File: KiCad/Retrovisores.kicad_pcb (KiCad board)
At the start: 2 copper layers, 68 parts, among them J1 Conn_01x02_Pin, J10 Conn_01x07_Pin, J11 Conn_01x02_Pin, J2 DE9_Pins, J3 Conn_01x04_Pin, J4 DE9_Pins, J5 Conn_01x02_Pin, J6 Conn_01x02_Pin, J7 Conn_01x02_Pin, J8 Conn_PIC_ICSP_ICD, J9 Conn_01x04_Pin, K2 Relay_SPDT, Q14 AO3400A, Q15 AO3401A, Q16 AO3400A, Q17 AO3401A, Q18 AO3400A, Q19 AO3401A, Q20 AO3400A, Q21 AO3401A, Q22 AO3400A, Q23 AO3401A, Q24 AO3400A, Q25 AO3401A, Q27 AO3400A, SW1 SW_Push, SW2 SW_Push, SW3 SW_Push, SW4 SW_Push, SW6 SW_Nidec_CAS-120A1, U2 SN65HVD232, U4 LT1117-3.3, U5 TSR3-2450N, U7 PIC32MX250F128D-IPT, Y1 Crystal

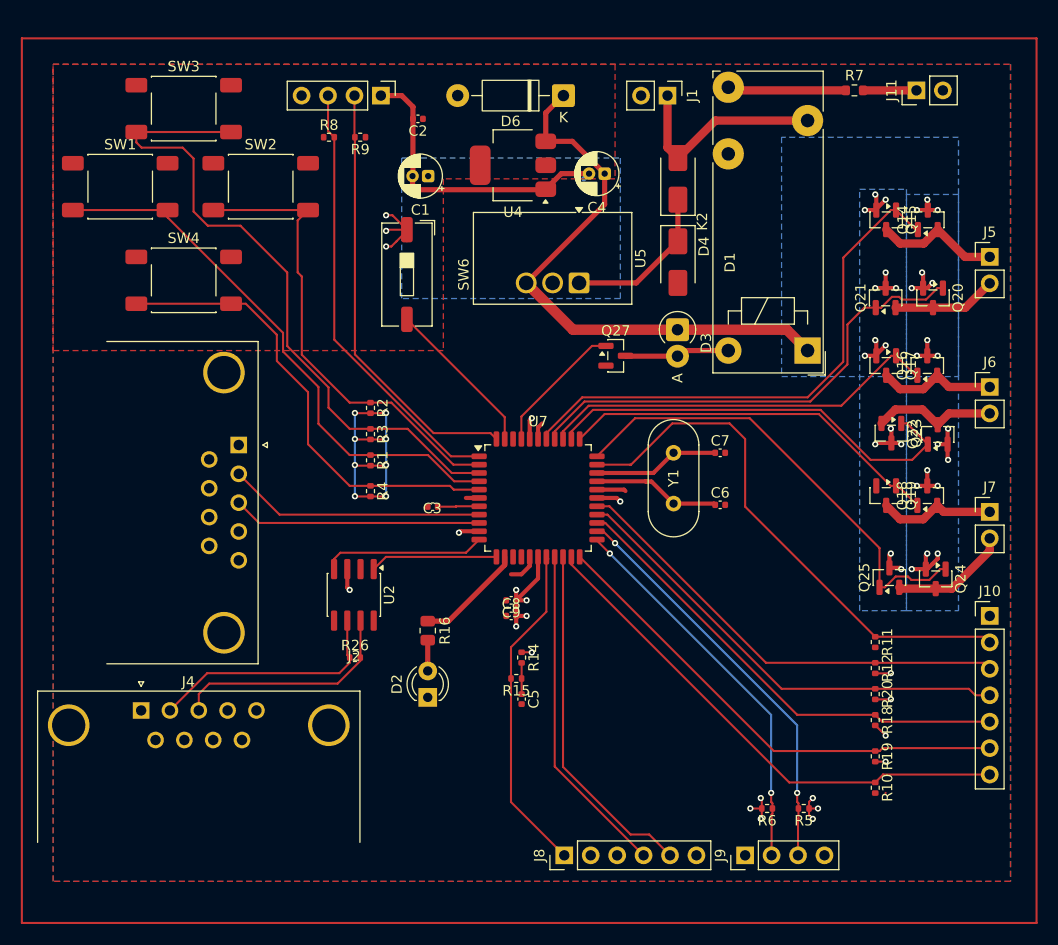
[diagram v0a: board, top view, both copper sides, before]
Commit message: habia un par de cosas mal en las reglas de diseño
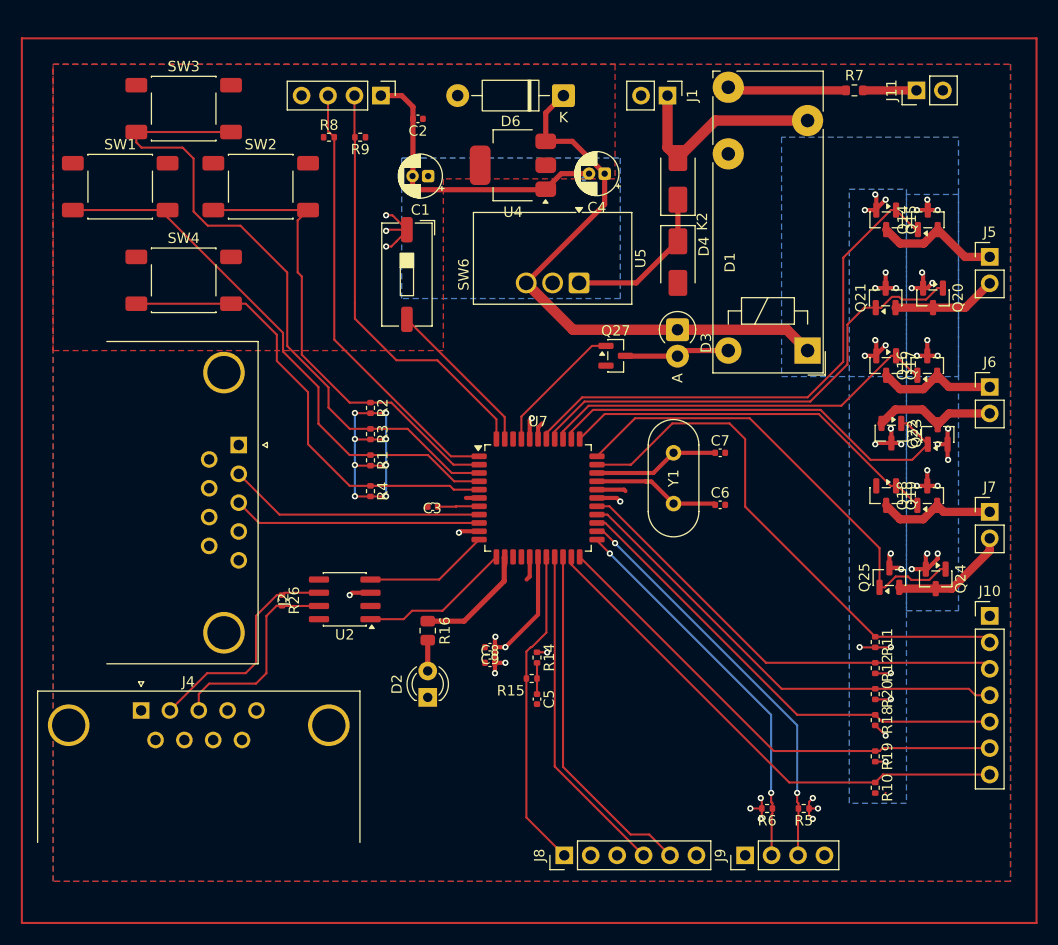
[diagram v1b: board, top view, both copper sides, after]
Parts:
- moved R26 8.90 mm to (110.0, 79.0), turned to -90 degrees
- moved C8 4.94 mm to (130.0, 85.0)
- moved C9 4.94 mm to (130.0, 83.5)
- moved R15 1.48 mm to (134.0, 86.5)
- moved C5 1.48 mm to (134.5, 88.5)
- moved R14 1.48 mm to (134.5, 84.5)
- moved U2 0.98 mm to (116.0, 78.9), turned to 180 degrees
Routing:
- net VCC: track 35.0 -> 39.9 mm
- net U: track 68.5 -> 64.5 mm
- net DCAN: track 15.7 -> 12.0 mm
- net Net-(U2-CANH): track 22.3 -> 19.9 mm
- net GND: track 90.0 -> 92.3 mm, vias 26 -> 28
- net RCAN: track 12.3 -> 14.6 mm
- net Net-(U2-CANL): track 23.3 -> 21.6 mm
- net Net-(U7-RA7): track 10.4 -> 12.1 mm
- net MCLR: track 32.5 -> 31.3 mm
- net KLKI2C: track 41.9 -> 41.0 mm

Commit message: ajustado ancho de pista de Vbat y 5V
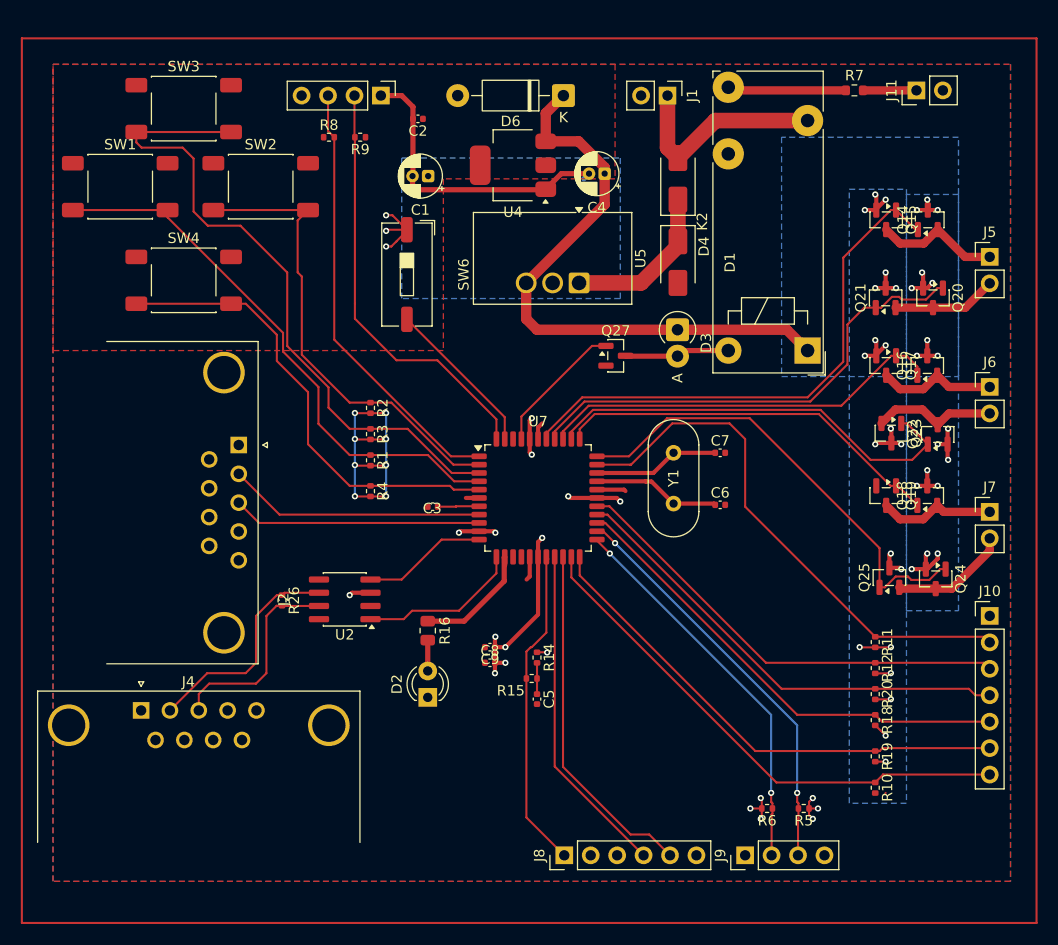
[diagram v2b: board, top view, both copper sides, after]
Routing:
- net VCC: track 39.9 -> 47.9 mm, vias 18 -> 22
- net 5V: track 78.2 -> 80.6 mm
- net FC5: track 47.2 -> 48.3 mm
- net RCAN: track 14.6 -> 15.5 mm
- net FC6: track 49.9 -> 50.7 mm
- net SDU1: track 38.6 -> 39.2 mm
- net OP: track 37.1 -> 37.6 mm

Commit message: versión casi final del enrutado
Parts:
- removed R7: 4.7k, Resistor_SMD:R_0603_1608Metric
- moved J8 12.9 mm to (125.5, 98.0)
- moved R5 12.4 mm to (149.0, 93.5)
- moved R6 12.4 mm to (145.5, 93.5)
- moved J9 11.4 mm to (144.5, 98.0)
- moved C2 7.76 mm to (123.5, 40.5), turned to -90 degrees
- moved J4 4.53 mm to (101.0, 89.1)
- moved SW1 4.12 mm to (98.5, 40.2)
- moved SW2 4.12 mm to (112.0, 40.2)
- moved SW3 4.12 mm to (104.5, 32.8)
- moved SW4 4.12 mm to (104.5, 49.2)
- moved J11 3.96 mm to (167.0, 30.0)
- moved C1 3.78 mm to (126.0, 35.0)
- moved J3 3.12 mm to (122.6, 30.5)
- moved R8 3.12 mm to (117.6, 34.5)
- moved R9 3.12 mm to (120.6, 34.5)
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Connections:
- net Net-(U2-CANH) renamed CAN_+
- net Net-(U2-CANL) renamed CAN_-
- K2 pad 14: Net-(K2-Pad14) -> Net-(J11-Pin_1)
- Q14 pad 3: 5V -> VBAT
- Q16 pad 3: 5V -> VBAT
- Q18 pad 3: 5V -> VBAT
- Q20 pad 2: 5V -> VBAT
- Q22 pad 2: 5V -> VBAT
- Q24 pad 2: 5V -> VBAT
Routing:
- net 5V: track 80.6 -> 55.5 mm, vias 18 -> 0
- net VBAT: track 20.4 -> 44.1 mm, vias 0 -> 18
- net GND: track 92.3 -> 71.4 mm, vias 28 -> 31
- net Net-(K2-Pad14): track 11.4 -> 0.00 mm
- net PGC: track 34.0 -> 23.7 mm
- net SCL: track 39.5 -> 29.8 mm
- net SDA: track 37.4 -> 28.1 mm
- net Net-(J11-Pin_1): track 5.14 -> 14.2 mm
- net PGD: track 32.2 -> 24.5 mm
- net CAN_-: track 21.6 -> 16.9 mm
- net L: track 45.0 -> 40.9 mm
- net MCLR: track 31.3 -> 27.6 mm
- net D: track 44.7 -> 41.3 mm
- net CAN_+: track 19.9 -> 16.7 mm
- net RX: track 24.7 -> 27.1 mm
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- added copper zone on B.Cu, net VBAT
- removed copper zone on B.Cu, net 5V
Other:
- board outline added: 92 x 77 mm

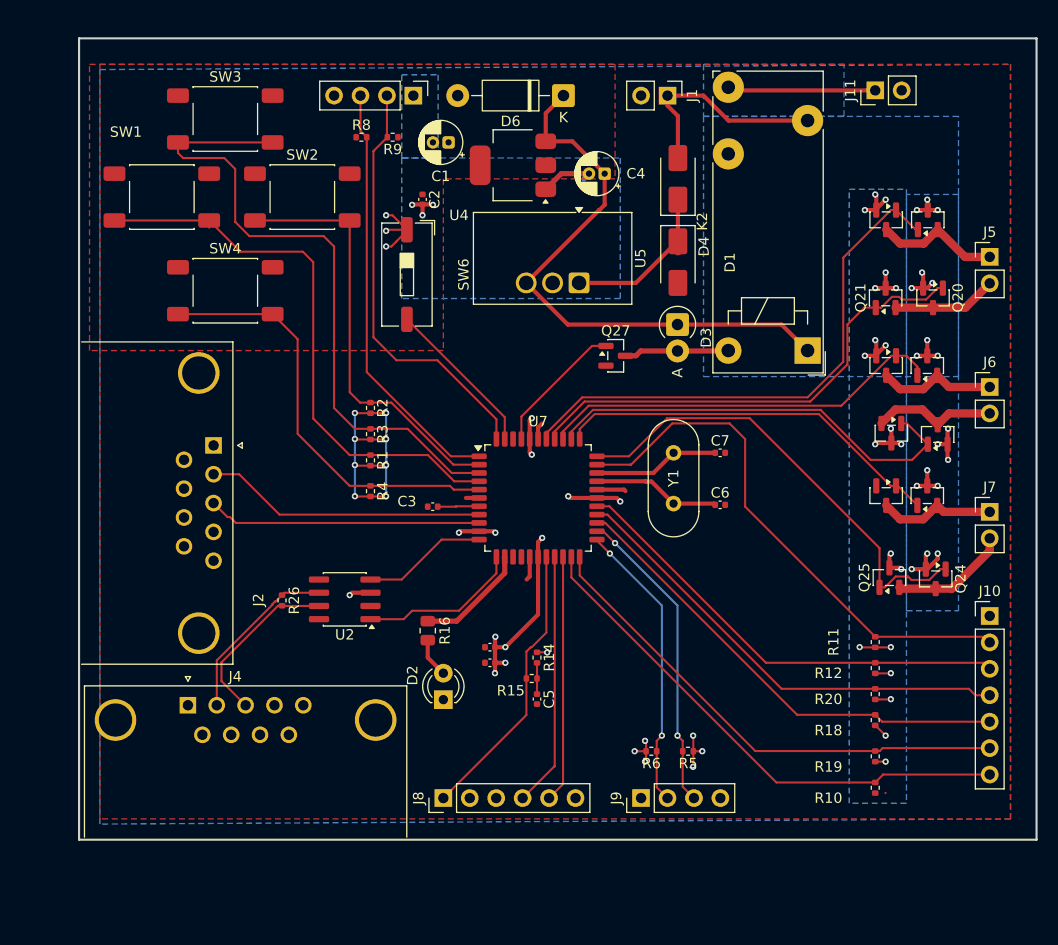
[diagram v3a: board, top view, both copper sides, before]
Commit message: añadido test points y solucionado un error con gnd en alimentación
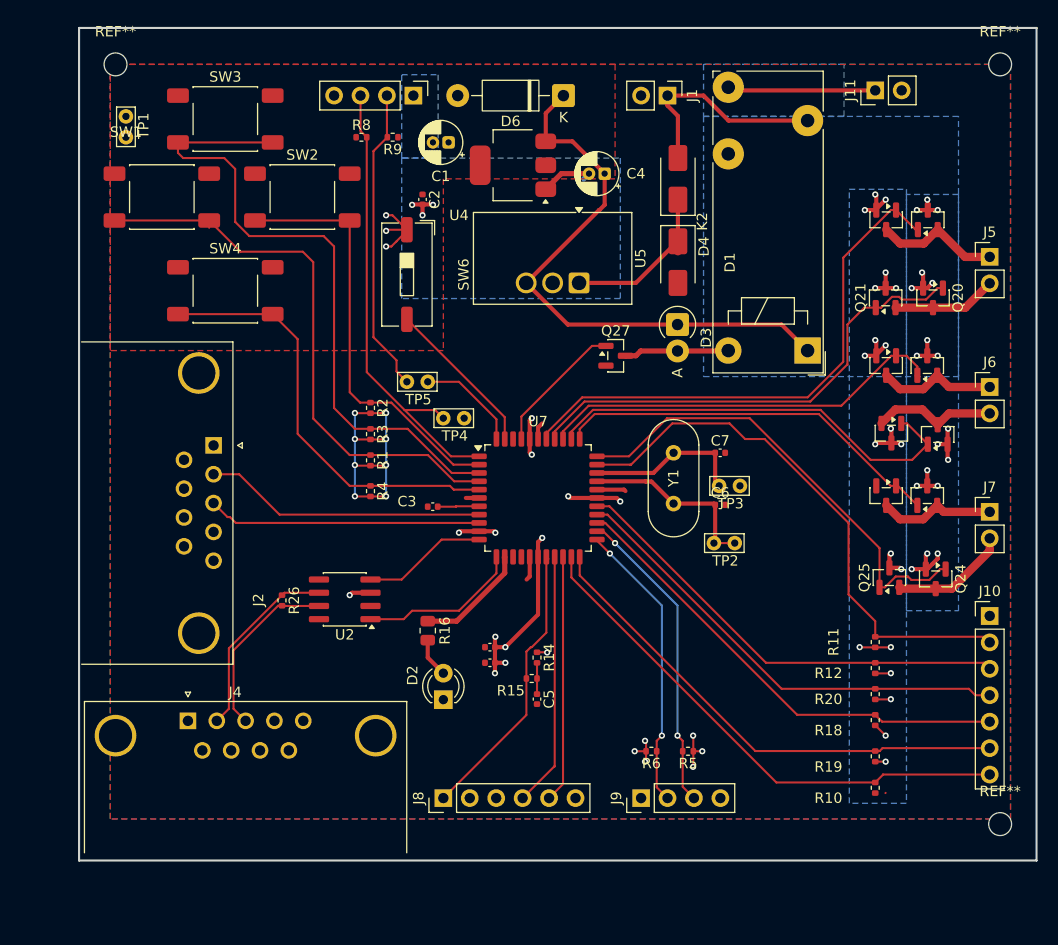
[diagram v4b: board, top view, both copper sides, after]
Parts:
- added REF**: MountingHole_2.2mm_M2, MountingHole:MountingHole_2.2mm_M2, F.Cu at (179.0, 100.5)
- added REF**: MountingHole_2.2mm_M2, MountingHole:MountingHole_2.2mm_M2, F.Cu at (94.0, 27.5)
- added REF**: MountingHole_2.2mm_M2, MountingHole:MountingHole_2.2mm_M2, F.Cu at (179.0, 27.5)
- added TP1: TestPoint, TestPoint:TestPoint_Bridge_Pitch2.0mm_Drill0.7mm, F.Cu at (95.0, 34.5)
- added TP2: TestPoint, TestPoint:TestPoint_Bridge_Pitch2.0mm_Drill0.7mm, F.Cu at (151.5, 73.5)
- added TP3: TestPoint, TestPoint:TestPoint_Bridge_Pitch2.0mm_Drill0.7mm, F.Cu at (152.0, 68.0)
- added TP4: TestPoint, TestPoint:TestPoint_Bridge_Pitch2.0mm_Drill0.7mm, F.Cu at (125.5, 61.5)
- added TP5: TestPoint, TestPoint:TestPoint_Bridge_Pitch2.0mm_Drill0.7mm, F.Cu at (122.0, 58.0)
- moved J4 1.50 mm to (101.0, 90.6)
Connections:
- J1 pad 2: GNDPWR -> GND
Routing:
- net OSC1: track 12.3 -> 18.7 mm
- net DI2C: track 41.0 -> 45.0 mm
- net OSC2: track 12.2 -> 15.5 mm
- net CAN_-: track 16.9 -> 18.3 mm
- net KLKI2C: track 40.8 -> 39.4 mm
- net FCR: track 51.9 -> 53.0 mm
- net CAN_+: track 16.7 -> 17.3 mm
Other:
- board size 92 x 77 mm -> 92 x 80 mm

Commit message: Eliminado los errores del DRC
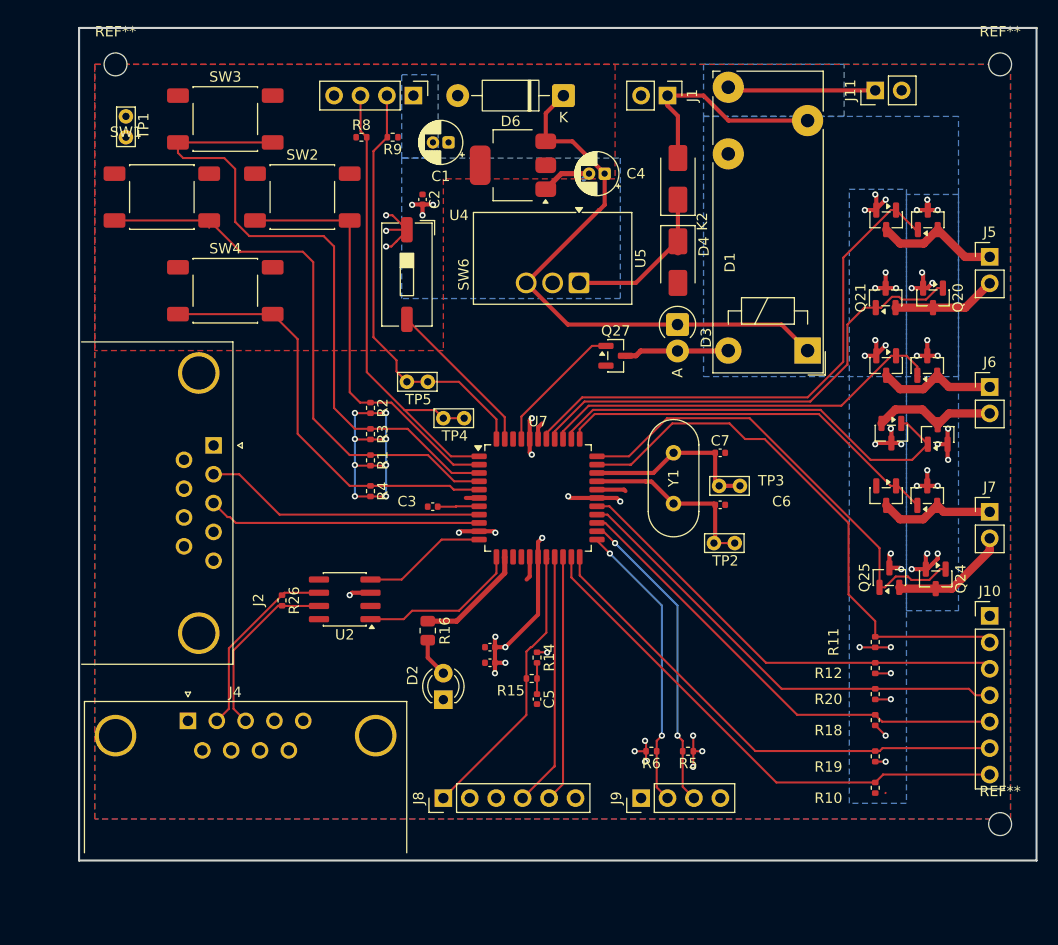
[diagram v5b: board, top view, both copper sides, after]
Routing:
- net OSC2: track 15.5 -> 17.5 mm
- net KLKI2C: track 39.4 -> 41.4 mm
- net DI2C: track 45.0 -> 47.0 mm
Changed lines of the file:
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@@
 		(tags "capacitor")
 		(property "Reference" "C6"
-			(at 0 -1.16 0)
+			(at 5.9 -0.325 0)
 			(layer "F.SilkS")
 			(effects
@@
 		(tags "test point wire loop")
 		(property "Reference" "TP3"
-			(at 1.1 1.7 0)
+			(at 5 -0.5 0)
 			(layer "F.SilkS")
 			(effects
@@
 	)
 	(segment
-		(start 151.62 67.62)
-		(end 152 68)
+		(start 152 68)
+		(end 154 68)
 		(width 0.4)
 		(layer "F.Cu")
@@
 	)
 	(segment
+		(start 151.62 67.62)
+		(end 152 68)
+		(width 0.4)
+		(layer "F.Cu")
+		(net 7)
+	)
+	(segment
 		(start 145.6825 66.7625)
 		(end 140.2625 66.7625)
@@
 	)
 	(segment
+		(start 125.5 61.5)
+		(end 127.5 61.5)
+		(width 0.2)
+		(layer "F.Cu")
+		(net 53)
+	)
+	(segment
 		(start 117.54 33.9)
 		(end 118.14 34.5)
@@
 	)
 	(segment
+		(start 122 58)
+		(end 124 58)
+		(width 0.2)
+		(layer "F.Cu")
+		(net 54)
+	)
+	(segment
 		(start 130.6 63.5)
 		(end 130.6 61.6)
@@
 		(polygon
 			(pts
-				(xy 93.5 27.5) (xy 180 27.5) (xy 180 100) (xy 93.5 100)
+				(xy 92 27.5) (xy 180 27.5) (xy 180 100) (xy 92 100)
 			)
 		)
@@
 		(polygon
 			(pts
-				(xy 93.5 27.5) (xy 142 27.5) (xy 142 38.5) (xy 125.5 38.5) (xy 125.5 55) (xy 93.5 55)
+				(xy 92 27.5) (xy 142 27.5) (xy 142 38.5) (xy 125.5 38.5) (xy 125.5 55) (xy 92 55)
 			)
 		)
@@
 		(polygon
 			(pts
-				(xy 93.5 27.5) (xy 180 27.5) (xy 180 100) (xy 93.5 100)
+				(xy 92 27.5) (xy 180 27.5) (xy 180 100) (xy 92 100)
 			)
 		)

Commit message: ultima versió PCB
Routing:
- net VBAT: track 44.1 -> 42.1 mm
- net Net-(D1-K): track 16.6 -> 15.2 mm
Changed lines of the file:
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@@
 	)
 	(segment
-		(start 148.04 44.5)
-		(end 148.04 44.96)
-		(width 1.5)
-		(layer "F.Cu")
-		(net 8)
-	)
-	(segment
-		(start 148 44.5)
-		(end 144 48.5)
-		(width 0.4)
-		(layer "F.Cu")
-		(net 8)
-	)
-	(segment
-		(start 144 48.5)
-		(end 138.54 48.5)
-		(width 0.4)
-		(layer "F.Cu")
-		(net 8)
-	)
-	(segment
-		(start 148.04 44.5)
-		(end 148.04 45.46)
-		(width 0.8)
+		(start 138.54 48.5)
+		(end 144.04 48.5)
+		(width 1)
 		(layer "F.Cu")
 		(net 8)
@@
 		(start 148.04 40.5)
 		(end 148.04 44.5)
-		(width 0.4)
+		(width 1)
 		(layer "F.Cu")
 		(net 8)
@@
 	)
 	(segment
+		(start 144.04 48.5)
+		(end 148.04 44.5)
+		(width 1)
+		(layer "F.Cu")
+		(net 8)
+	)
+	(segment
 		(start 171.6 47.6)
 		(end 171.5 47.5)
@@
 	)
 	(segment
-		(start 152.9 32.9)
-		(end 150.5 30.5)
-		(width 0.4)
-		(layer "F.Cu")
-		(net 9)
-	)
-	(segment
 		(start 171.6 49)
 		(end 171.6 47.6)
@@
 		(end 171 41.5)
 		(width 0.4)
+		(layer "F.Cu")
+		(net 9)
+	)
+	(segment
+		(start 147.04 32.04)
+		(end 148.04 33.04)
+		(width 1)
 		(layer "F.Cu")
 		(net 9)
@@
 	)
 	(segment
+		(start 151 32.9)
+		(end 160.5 32.9)
+		(width 1)
+		(layer "F.Cu")
+		(net 9)
+	)
+	(segment
 		(start 173.95 65.45)
 		(end 174 65.5)
@@
 	)
 	(segment
-		(start 148.04 32.46)
-		(end 148.04 36.5)
-		(width 0.4)
-		(layer "F.Cu")
-		(net 9)
-	)
-	(segment
 		(start 172.05 41.5)
 		(end 172.05 40.55)
@@
 	)
 	(segment
-		(start 160.5 32.9)
-		(end 152.9 32.9)
-		(width 0.4)
-		(layer "F.Cu")
-		(net 9)
-	)
-	(segment
 		(start 173.95 62.55)
 		(end 174 62.5)
@@
 	)
 	(segment
-		(start 147.04 31.46)
-		(end 148.04 32.46)
-		(width 0.4)
-		(layer "F.Cu")
-		(net 9)
-	)
-	(segment
 		(start 172.05 40.55)
 		(end 172 40.5)
@@
 	)
 	(segment
-		(start 150.5 30.5)
-		(end 147.04 30.5)
-		(width 0.4)
-		(layer "F.Cu")
-		(net 9)
-	)
-	(segment
 		(start 171.860266 76)
 		(end 171.860266 74.639734)
@@
 	)
 	(segment
+		(start 148.04 33.04)
+		(end 148.04 36.5)
+		(width 1)
+		(layer "F.Cu")
+		(net 9)
+	)
+	(segment
 		(start 172.05 41.5)
 		(end 173 41.5)
@@
 	)
 	(segment
+		(start 150.86 33.04)
+		(end 151 32.9)
+		(width 1)
+		(layer "F.Cu")
+		(net 9)
+	)
+	(segment
 		(start 173.95 64)
 		(end 173.95 62.55)
@@
 	)
 	(segment
+		(start 147.04 30.5)
+		(end 147.04 32.04)
+		(width 1)
+		(layer "F.Cu")
+		(net 9)
+	)
+	(segment
+		(start 148.04 33.04)
+		(end 150.86 33.04)
+		(width 1)
+		(layer "F.Cu")
+		(net 9)
+	)
+	(segment
 		(start 173 75)
 		(end 173 74.5)
 		(width 0.4)
 		(layer "F.Cu")
-		(net 9)
-	)
-	(segment
-		(start 147.04 30.5)
-		(end 147.04 31.46)
-		(width 0.4)
-		(layer "F.Cu")
